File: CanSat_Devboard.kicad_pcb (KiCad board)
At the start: 4 copper layers, 64.1 x 43.6 mm, 49 parts, among them IC1 114993390, J1 I2C, J3 Conn_01x03_Pin, J4 USB_C_Receptacle_USB2.0_16P, J5 693071010811, J6 SWD, J7 RMF, J8 GPIO, SW3 SW_Push, SW4 SHPHLD, SW5 RST, U1 E73-2G4M08S1C, U3 SRV05-4, U4 NPM1300-QEAA-R7, Y1 32.768

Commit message: Flipped SD card slot
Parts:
- moved R1 14.1 mm to (179.2, 103.3)
- moved R3 13.3 mm to (179.2, 97.2)
- moved C3 12.8 mm to (179.2, 101.7)
- moved R2 12.4 mm to (179.2, 98.7)
- moved C4 12.3 mm to (179.2, 100.2)
- moved J5 6.74 mm to (172.6, 98.3), turned to 90 degrees
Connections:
- U1 pad 33: CS -> MISO
- U1 pad 35: MOSI -> SCK
- U1 pad 41: SCK -> MOSI
- U1 pad 43: MISO -> CS
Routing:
- net CS: track 26.0 -> 41.1 mm
- net MOSI: track 26.6 -> 40.9 mm
- net +3.3V: track 103.0 -> 115.2 mm
- net MISO: track 28.6 -> 38.8 mm
- net SCK: track 27.8 -> 37.2 mm
- net GND: track 7.20 -> 6.43 mm, vias 82 -> 84

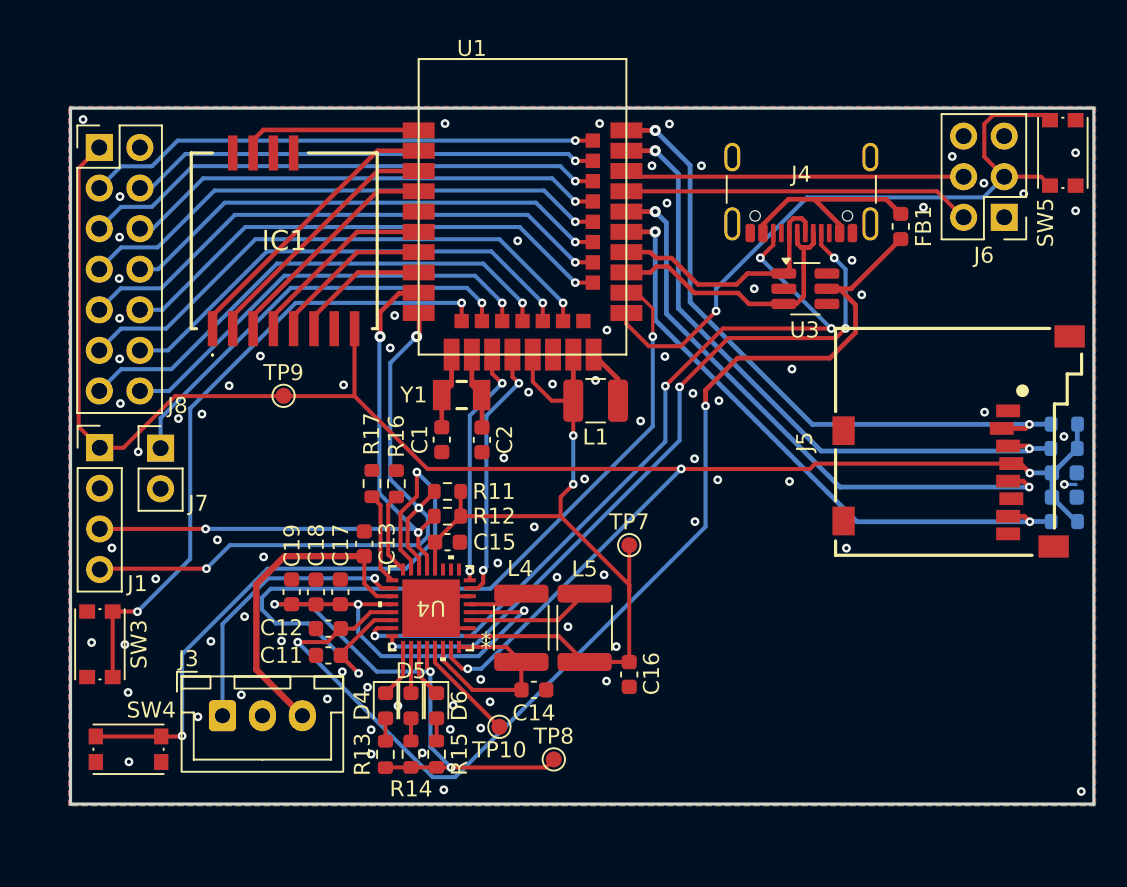
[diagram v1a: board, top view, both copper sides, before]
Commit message: Connected DIO1 of lora module
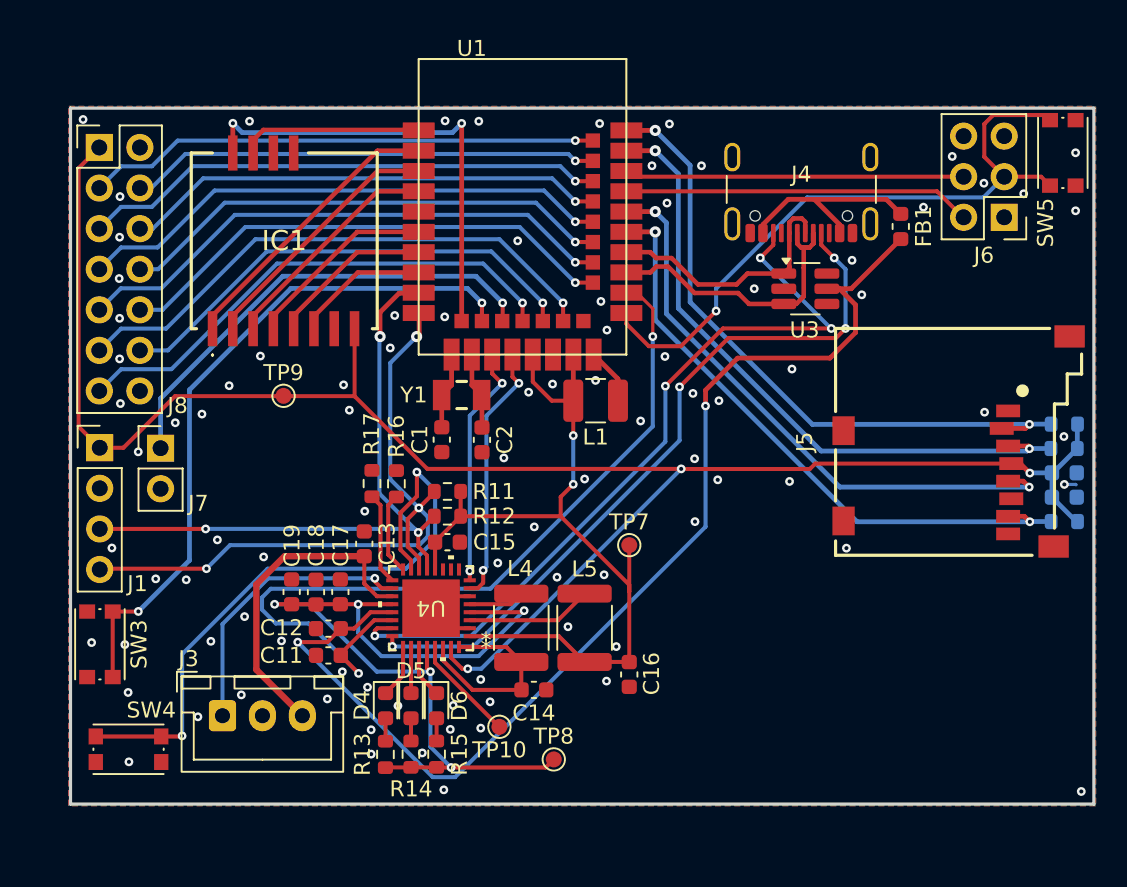
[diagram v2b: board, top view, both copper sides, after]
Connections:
- IC1 pad 12: unconnected-(IC1-DIO1-Pad12) -> LoRa_DIO1
- J4 pad SH: GND -> (no net)
- U1 pad 12: SW0 -> LoRa_DIO1
- U1 pad 14: RMF -> SW0
- U1 pad 16: 0.08 -> RMF
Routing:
- net LoRa_DIO1: track 0.00 -> 29.0 mm, vias 0 -> 2
- net 0.08: track 27.5 -> 0.00 mm, vias 1 -> 0
- net SW0: track 40.6 -> 43.1 mm
- net RMF: track 26.9 -> 29.3 mm
- net GND: vias 84 -> 91
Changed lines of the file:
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@@
 			(layers "*.Cu" "*.Mask" "F.Paste")
 			(remove_unused_layers no)
-			(net "GND")
 		)
 		(pad "SH" thru_hole oval
@@
 			(layers "*.Cu" "*.Mask" "F.Paste")
 			(remove_unused_layers no)
-			(net "GND")
 		)
 		(pad "SH" thru_hole oval
@@
 			(layers "*.Cu" "*.Mask" "F.Paste")
 			(remove_unused_layers no)
-			(net "GND")
 		)
 		(pad "SH" thru_hole oval
@@
 			(layers "*.Cu" "*.Mask" "F.Paste")
 			(remove_unused_layers no)
-			(net "GND")
 		)
 		(embedded_fonts no)
@@
 			(size 0.6 2.2)
 			(layers "F.Cu" "F.Mask" "F.Paste")
-			(net "unconnected-(IC1-DIO1-Pad12)")
+			(net "LoRa_DIO1")
 			(pinfunction "DIO1_12")
-			(pintype "passive+no_connect")
+			(pintype "passive")
 		)
 		(embedded_fonts no)
@@
 			(size 0.9 0.9)
 			(layers "F.Cu" "F.Mask" "F.Paste")
-			(net "SW0")
+			(net "LoRa_DIO1")
 			(pinfunction "P0.26_12")
 			(pintype "bidirectional")
@@
 			(size 0.9 0.9)
 			(layers "F.Cu" "F.Mask" "F.Paste")
-			(net "RMF")
+			(net "SW0")
 			(pinfunction "P0.06_14")
 			(pintype "bidirectional")
@@
 			(size 0.9 0.9)
 			(layers "F.Cu" "F.Mask" "F.Paste")
-			(net "0.08")
+			(net "RMF")
 			(pinfunction "P0.08_16")
 			(pintype "bidirectional")
@@
 	)
 	(via
+		(at 140.4286 78.187)
+		(size 0.55)
+		(drill 0.25)
+		(layers "F.Cu" "B.Cu")
+		(free yes)
+		(net "GND")
+	)
+	(via
 		(at 124.955 115.4912)
 		(size 0.55)
@@
 	)
 	(via
-		(at 140.4236 78.3564)
+		(at 179.8952 80.1852)
 		(size 0.55)
 		(drill 0.25)
@@
 	)
 	(via
-		(at 179.8952 80.1852)
+		(at 120.0528 85.4684)
 		(size 0.55)
 		(drill 0.25)
@@
 	)
 	(via
-		(at 120.0528 85.4684)
+		(at 140.7538 116.2786)
 		(size 0.55)
 		(drill 0.25)
@@
 	)
 	(via
-		(at 140.7538 116.2786)
+		(at 152.6664 96.9746)
 		(size 0.55)
 		(drill 0.25)
@@
 	)
 	(via
-		(at 152.6664 96.9746)
+		(at 134.4342 96.2972)
 		(size 0.55)
 		(drill 0.25)
@@
 	)
 	(via
-		(at 123.7358 96.8222)
+		(at 123.5376 97.0846)
 		(size 0.55)
 		(drill 0.25)
@@
 	)
 	(via
+		(at 124.2234 106.9144)
+		(size 0.55)
+		(drill 0.25)
+		(layers "F.Cu" "B.Cu")
+		(free yes)
+		(net "GND")
+	)
+	(via
 		(at 155.943 95.2474)
 		(size 0.55)
@@
 	)
 	(via
+		(at 142.5368 78.2124)
+		(size 0.55)
+		(drill 0.25)
+		(layers "F.Cu" "B.Cu")
+		(free yes)
+		(net "GND")
+	)
+	(via
 		(at 180.2508 120.1648)
 		(size 0.55)
@@
 	)
 	(via
+		(at 140.4032 90.4552)
+		(size 0.55)
+		(drill 0.25)
+		(layers "F.Cu" "B.Cu")
+		(free yes)
+		(net "GND")
+	)
+	(via
 		(at 137.4772 114.8054)
 		(size 0.55)
@@
 	)
 	(via
+		(at 150.1822 89.49)
+		(size 0.55)
+		(drill 0.25)
+		(layers "F.Cu" "B.Cu")
+		(free yes)
+		(net "GND")
+	)
+	(via
+		(at 135.3994 102.6218)
+		(size 0.55)
+		(drill 0.25)
+		(layers "F.Cu" "B.Cu")
+		(free yes)
+		(net "GND")
+	)
+	(via
 		(at 143.243 114.5514)
 		(size 0.55)
@@
 	)
 	(via
+		(at 128.1858 78.2124)
+		(size 0.55)
+		(drill 0.25)
+		(layers "F.Cu" "B.Cu")
+		(free yes)
+		(net "GND")
+	)
+	(via
 		(at 140.9316 114.78)
 		(size 0.55)
@@
 	)
 	(segment
-		(start 144.0058 89.7872)
-		(end 144.0058 90.6812)
-		(width 0.254)
-		(layer "F.Cu")
-		(net "0.08")
-	)
-	(segment
-		(start 144.005 89.7864)
-		(end 144.0058 89.7872)
-		(width 0.254)
-		(layer "F.Cu")
-		(net "0.08")
-	)
-	(segment
-		(start 144.005 89.5832)
-		(end 144.005 89.7864)
-		(width 0.254)
-		(layer "F.Cu")
-		(net "0.08")
-	)
-	(via
-		(at 144.005 89.5832)
-		(size 0.55)
-		(drill 0.25)
-		(layers "F.Cu" "B.Cu")
-		(net "0.08")
-	)
-	(segment
-		(start 144.005 89.5832)
-		(end 142.3032 87.8814)
-		(width 0.254)
-		(layer "B.Cu")
-		(net "0.08")
-	)
-	(segment
-		(start 130.3652 87.8814)
-		(end 123.1516 95.095)
-		(width 0.254)
-		(layer "B.Cu")
-		(net "0.08")
-	)
-	(segment
-		(start 142.3032 87.8814)
-		(end 130.3652 87.8814)
-		(width 0.254)
-		(layer "B.Cu")
-		(net "0.08")
-	)
-	(segment
-		(start 123.1516 95.095)
-		(end 121.3228 95.095)
-		(width 0.254)
-		(layer "B.Cu")
-		(net "0.08")
-	)
-	(segment
 		(start 139.8948 115.584799)
 		(end 139.8948 117.007099)
@@
 	)
 	(segment
-		(start 141.465 89.5832)
-		(end 141.465 89.7864)
+		(start 142.7358 89.7872)
+		(end 142.7358 90.6812)
 		(width 0.254)
 		(layer "F.Cu")
@@
 	)
 	(segment
-		(start 121.1598 108.902)
-		(end 121.1704 108.9126)
+		(start 121.2198 108.902)
+		(end 121.2262 108.8956)
 		(width 0.254)
 		(layer "F.Cu")
@@
 	(segment
 		(start 119.6208 108.902)
-		(end 121.1598 108.902)
-		(width 0.254)
-		(layer "F.Cu")
-		(net "SW0")
-	)
-	(segment
-		(start 141.4658 89.7872)
-		(end 141.4658 90.6812)
-		(width 0.254)
-		(layer "F.Cu")
-		(net "SW0")
-	)
-	(segment
-		(start 141.465 89.7864)
-		(end 141.4658 89.7872)
+		(end 121.2198 108.902)
 		(width 0.254)
 		(layer "F.Cu")
@@
 	)
 	(via
-		(at 121.1704 108.9126)
+		(at 121.2262 108.8956)
 		(size 0.55)
 		(drill 0.25)
@@
 	)
 	(via
-		(at 141.465 89.5832)
+		(at 142.735 89.5832)
 		(size 0.55)
 		(drill 0.25)
@@
 	)
 	(segment
-		(start 141.465 89.5832)
-		(end 131.0764 89.5832)
-		(width 0.254)
+		(start 124.4266 105.6952)
+		(end 124.4266 95.0272)
+		(width 0.3)
 		(layer "B.Cu")
 		(net "SW0")
 	)
 	(segment
-		(start 124.4724 105.6106)
-		(end 121.1704 108.9126)
-		(width 0.254)
+		(start 121.2262 108.8956)
+		(end 124.4266 105.6952)
+		(width 0.3)
 		(layer "B.Cu")
 		(net "SW0")
 	)
 	(segment
-		(start 131.0764 89.5832)
-		(end 124.4724 96.1872)
-		(width 0.254)
+		(start 130.7766 88.6772)
+		(end 141.829 88.6772)
+		(width 0.3)
 		(layer "B.Cu")
 		(net "SW0")
 	)
 	(segment
-		(start 124.4724 96.1872)
-		(end 124.4724 105.6106)
-		(width 0.254)
+		(start 124.4266 95.0272)
+		(end 130.7766 88.6772)
+		(width 0.3)
 		(layer "B.Cu")
 		(net "SW0")
 	)
 	(segment
-		(start 142.7358 89.7872)
-		(end 142.7358 90.6812)
-		(width 0.254)
-		(layer "F.Cu")
-		(net "RMF")
-	)
-	(segment
-		(start 142.735 89.5832)
-		(end 142.735 89.7864)
-		(width 0.254)
-		(layer "F.Cu")
-		(net "RMF")
+		(start 141.829 88.6772)
+		(end 142.735 89.5832)
+		(width 0.3)
+		(layer "B.Cu")
+		(net "SW0")
 	)
 	(segment
-		(start 142.735 89.7864)
-		(end 142.7358 89.7872)
+		(start 144.0312 89.7872)
+		(end 144.0312 90.6812)
 		(width 0.254)
 		(layer "F.Cu")
@@
 	)
 	(via
-		(at 142.735 89.5832)
+		(at 144.0304 89.5832)
 		(size 0.55)
 		(drill 0.25)
@@
 	)
 	(segment
-		(start 122.6182 96.7968)
+		(start 122.6182 95.5656)
 		(end 122.6182 98.6764)
-		(width 0.254)
+		(width 0.3)
 		(layer "B.Cu")
 		(net "RMF")
 	)
 	(segment
-		(start 141.7952 88.6434)
-		(end 130.7716 88.6434)
-		(width 0.254)
+		(start 130.2686 87.9152)
+		(end 122.6182 95.5656)
+		(width 0.3)
 		(layer "B.Cu")
 		(net "RMF")
 	)
 	(segment
-		(start 130.7716 88.6434)
-		(end 122.6182 96.7968)
-		(width 0.254)
+		(start 142.3624 87.9152)
+		(end 130.2686 87.9152)
+		(width 0.3)
 		(layer "B.Cu")
 		(net "RMF")
 	)
 	(segment
-		(start 142.735 89.5832)
-		(end 141.7952 88.6434)
-		(width 0.254)
+		(start 144.0304 89.5832)
+		(end 142.3624 87.9152)
+		(width 0.3)
 		(layer "B.Cu")
 		(net "RMF")
@@
 		(net "Net-(D4-A)")
 	)
+	(segment
+		(start 141.465 78.3444)
+		(end 141.47 78.3394)
+		(width 0.3)
+		(layer "F.Cu")
+		(net "LoRa_DIO1")
+	)
+	(segment
+		(start 141.465 90.7174)
+		(end 141.465 78.3444)
+		(width 0.3)
+		(layer "F.Cu")
+		(net "LoRa_DIO1")
+	)
+	(segment
+		(start 127.1394 80.197)
+		(end 127.1394 78.3444)
+		(width 0.3)
+		(layer "F.Cu")
+		(net "LoRa_DIO1")
+	)
+	(segment
+		(start 127.1394 78.3444)
+		(end 127.1444 78.3394)
+		(width 0.3)
+		(layer "F.Cu")
+		(net "LoRa_DIO1")
+	)
+	(via
+		(at 141.465 78.3444)
+		(size 0.55)
+		(drill 0.25)
+		(layers "F.Cu" "B.Cu")
+		(net "LoRa_DIO1")
+	)
+	(via
+		(at 127.1444 78.3394)
+		(size 0.55)
+		(drill 0.25)
+		(layers "F.Cu" "B.Cu")
+		(net "LoRa_DIO1")
+	)
+	(segment
+		(start 140.8858 78.9236)
+		(end 127.7286 78.9236)
+		(width 0.3)
+		(layer "B.Cu")
+		(net "LoRa_DIO1")
+	)
+	(segment
+		(start 127.7286 78.9236)
+		(end 127.1444 78.3394)
+		(width 0.3)
+		(layer "B.Cu")
+		(net "LoRa_DIO1")
+	)
+	(segment
+		(start 141.465 78.3444)
+		(end 140.8858 78.9236)
+		(width 0.3)
+		(layer "B.Cu")
+		(net "LoRa_DIO1")
+	)
 	(zone

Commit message: Fixed a roouting mistake
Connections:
- J8 pad 14: 0.08 -> unconnected-(J8-Pin_14-Pad14)
- U4 pad 23: CC2 -> CC1
- U4 pad 24: CC1 -> CC2
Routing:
- net CC1: track 45.8 -> 48.7 mm
- net CC2: track 48.2 -> 46.4 mm
- net VSYS: track 55.1 -> 55.9 mm

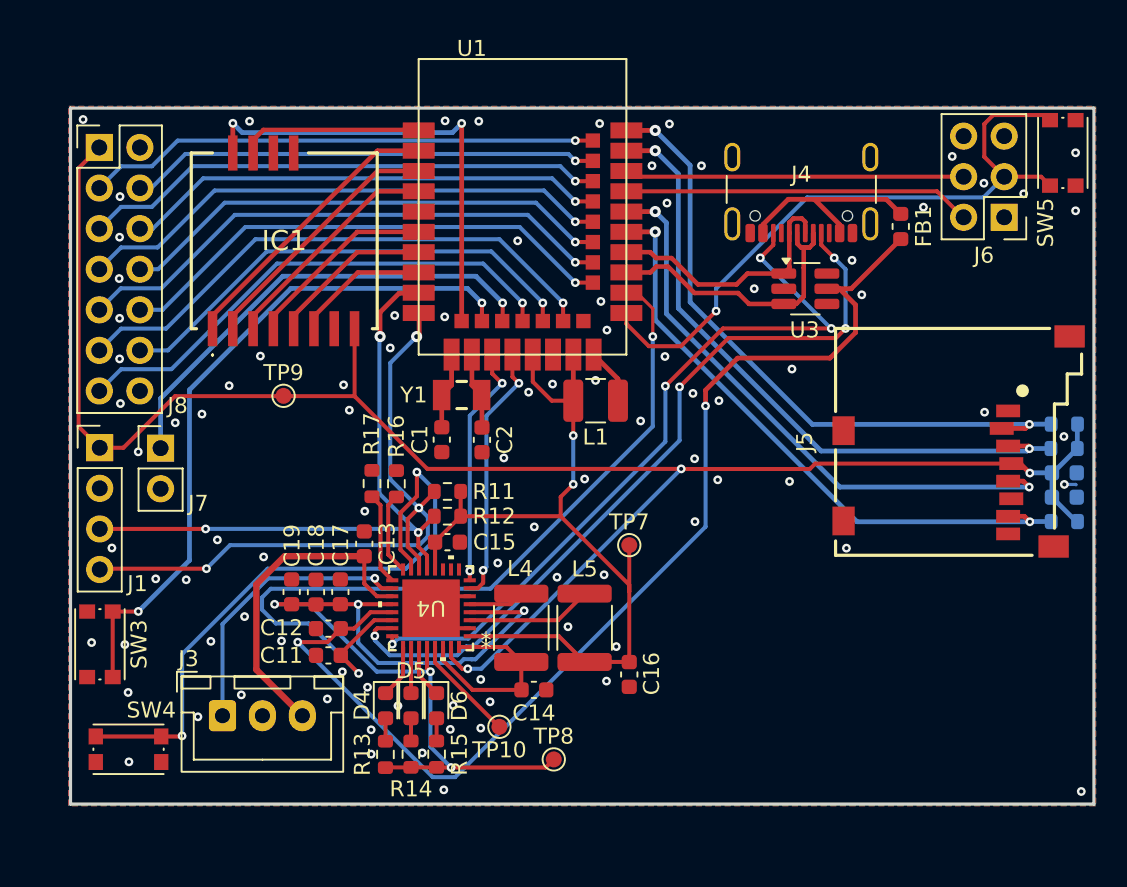
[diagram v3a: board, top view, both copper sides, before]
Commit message: Changed power routing and board color
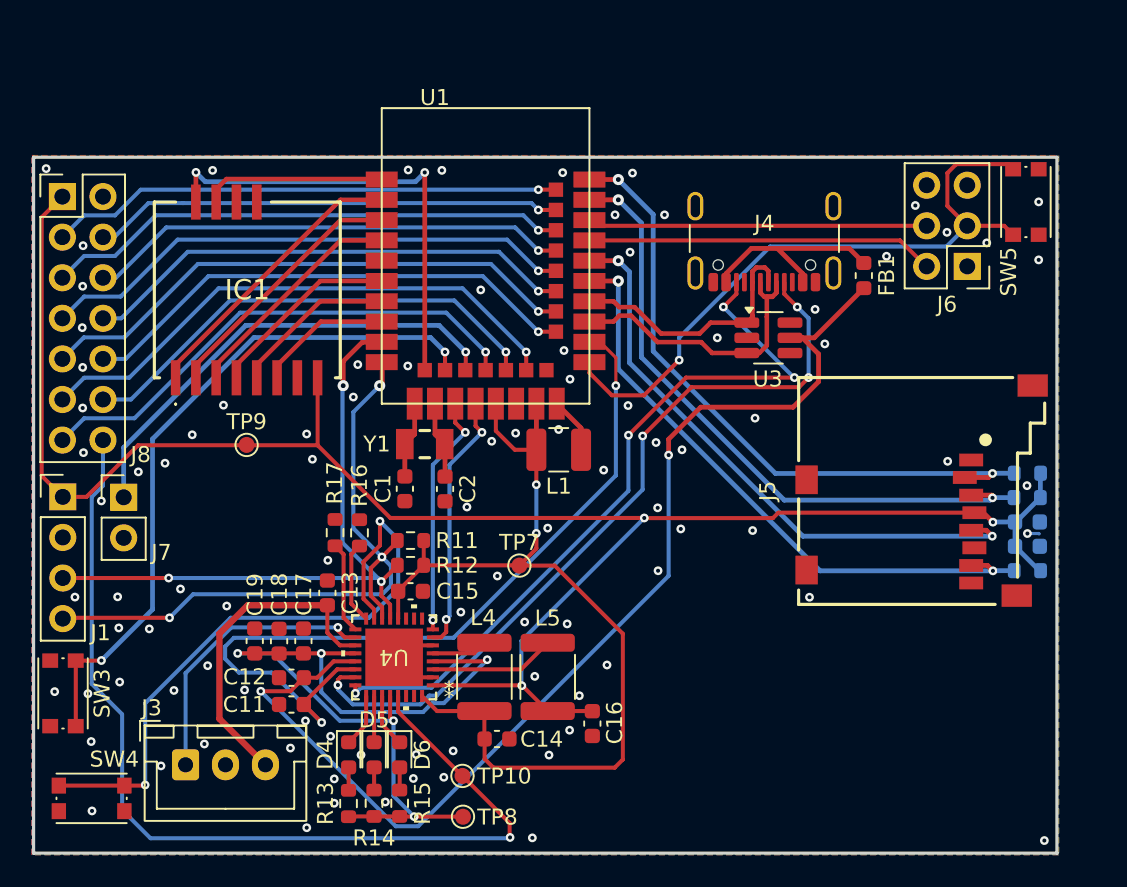
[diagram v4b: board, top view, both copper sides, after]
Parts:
- R16: value 150k -> 500k
- moved TP7 7.00 mm to (145.1, 106.0)
- moved TP8 6.72 mm to (141.5, 121.7)
- moved C2 3.85 mm to (140.4, 101.2)
- moved FB1 3.85 mm to (166.6, 87.9)
- moved L5 3.85 mm to (146.8, 113.0)
- moved TP9 3.85 mm to (128.0, 98.5)
- moved U4 3.85 mm to (137.2, 111.8)
- moved J1 3.85 mm to (116.5, 101.7)
- moved SW3 3.85 mm to (116.5, 114.0)
- moved C1 3.85 mm to (137.9, 101.2)
- moved D4 3.85 mm to (134.4, 117.9)
- moved J5 3.85 mm to (170.3, 101.4)
- moved C14 3.85 mm to (143.7, 116.9)
- moved C17 3.85 mm to (131.6, 110.7)
- moved C19 3.85 mm to (128.5, 110.7)
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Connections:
- C14 pad 1: VOUT2 -> VMCU
- C16 pad 2: VMCU -> +3.3V
- J8 pad 14: unconnected-(J8-Pin_14-Pad14) -> VLDO
- L4 pad 1: VOUT2 -> VMCU
- L5 pad 2: VMCU -> +3.3V
- U4 pad 1: VMCU -> +3.3V
- U4 pad 30: VOUT2 -> unconnected-(U4A-LSIN2/VINLDO2-Pad30)
- U4 pad 31: +3.3V -> unconnected-(U4A-LSOUT2/VOUTLDO2-Pad31)
- U4 pad 32: VOUT2 -> VMCU
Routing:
- net VLDO: track 7.00 -> 61.4 mm, vias 0 -> 1
- net VOUT2: track 12.6 -> 0.00 mm
- net VMCU: track 51.4 -> 59.8 mm
- net +3.3V: track 115.2 -> 119.0 mm
- net VSYS: track 55.9 -> 52.3 mm
- net GND: vias 91 -> 95
